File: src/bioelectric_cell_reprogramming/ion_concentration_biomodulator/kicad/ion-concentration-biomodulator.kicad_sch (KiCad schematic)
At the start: 54 parts, among them J1 532610671, J10 39-53-2045, J11 Conn_01x14_Pin, J12 Conn_01x14_Pin, J13 39-53-2045, J14 39-53-2045, J15 Conn_ARM_SWD_TagConnect_TC2030, J16 IPL1-104-01-L-D-K, J17 Conn_01x02_Pin, J18 EJ508A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

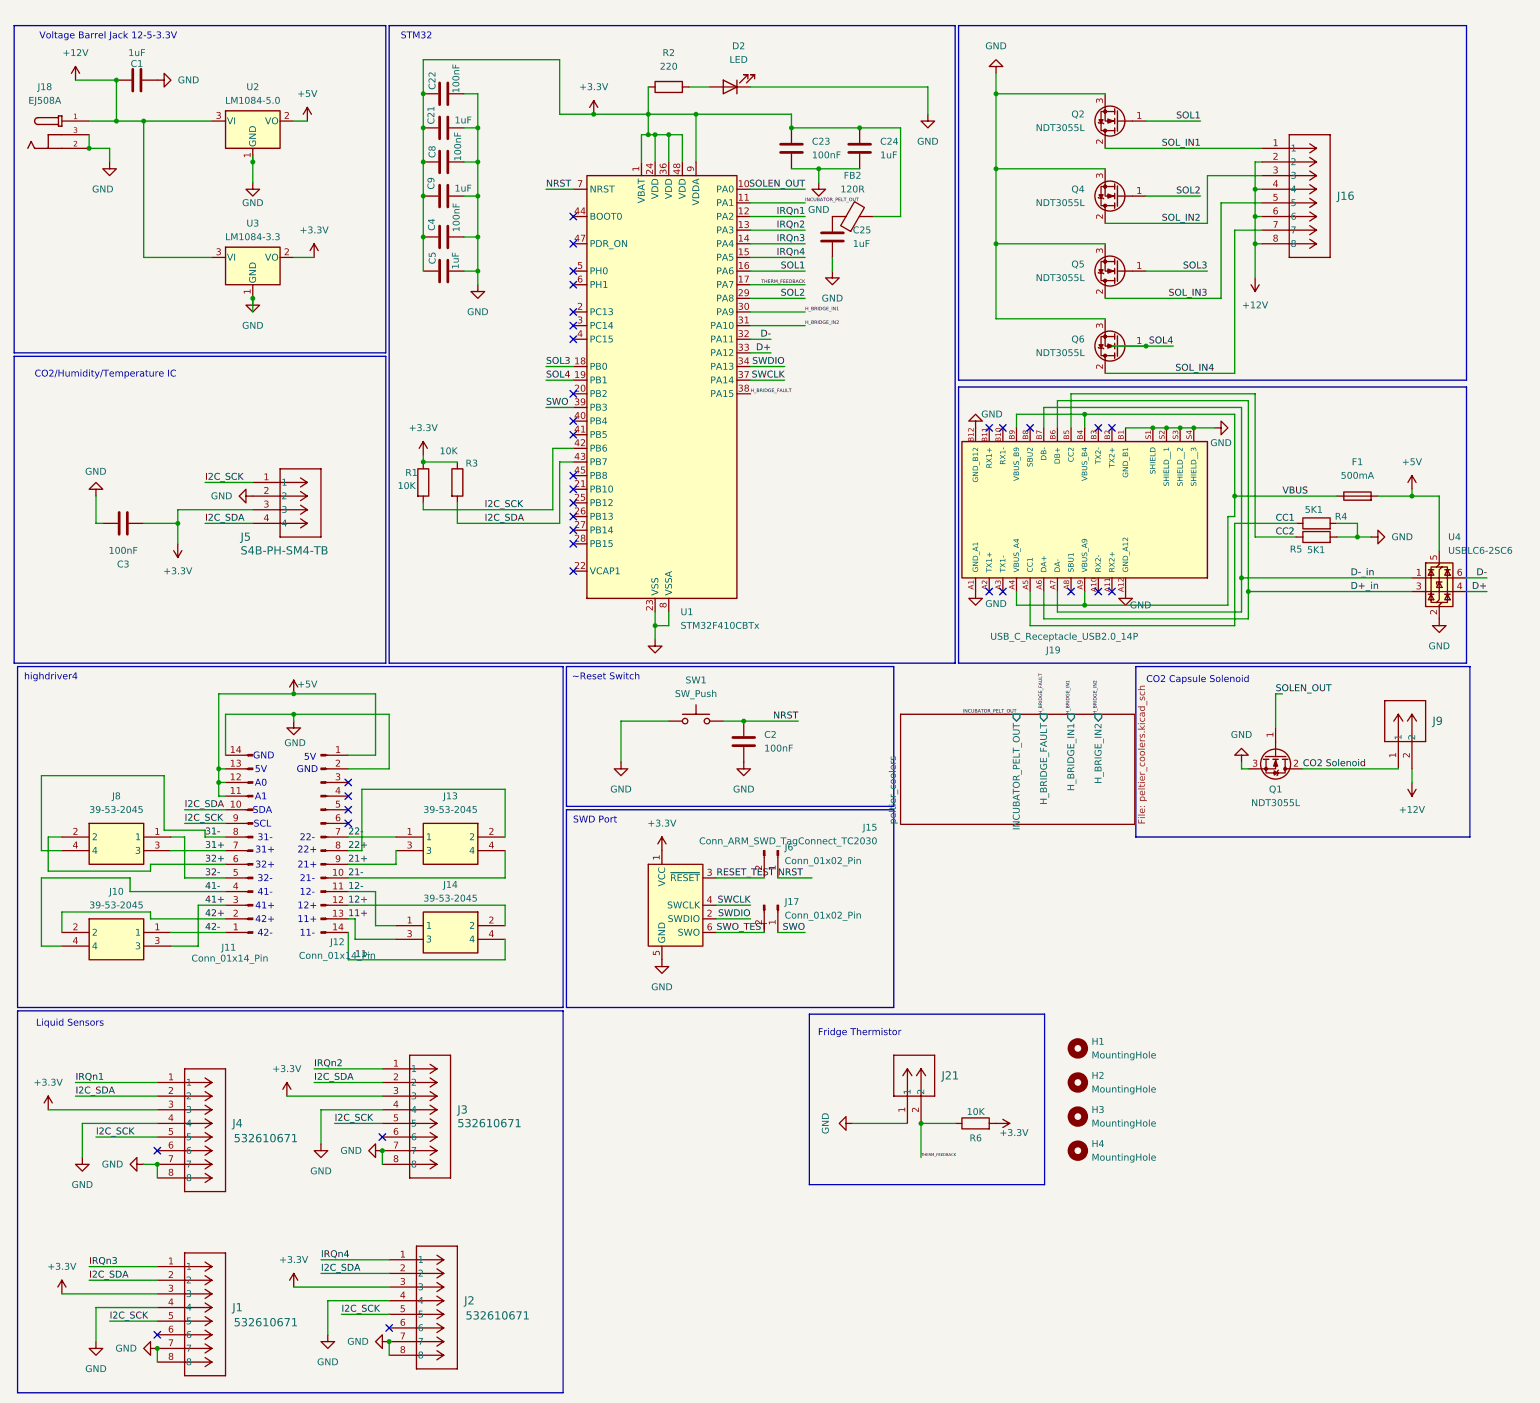
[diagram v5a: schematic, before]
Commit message: fix: bigger STM32, fix mirrored highdriver pinout
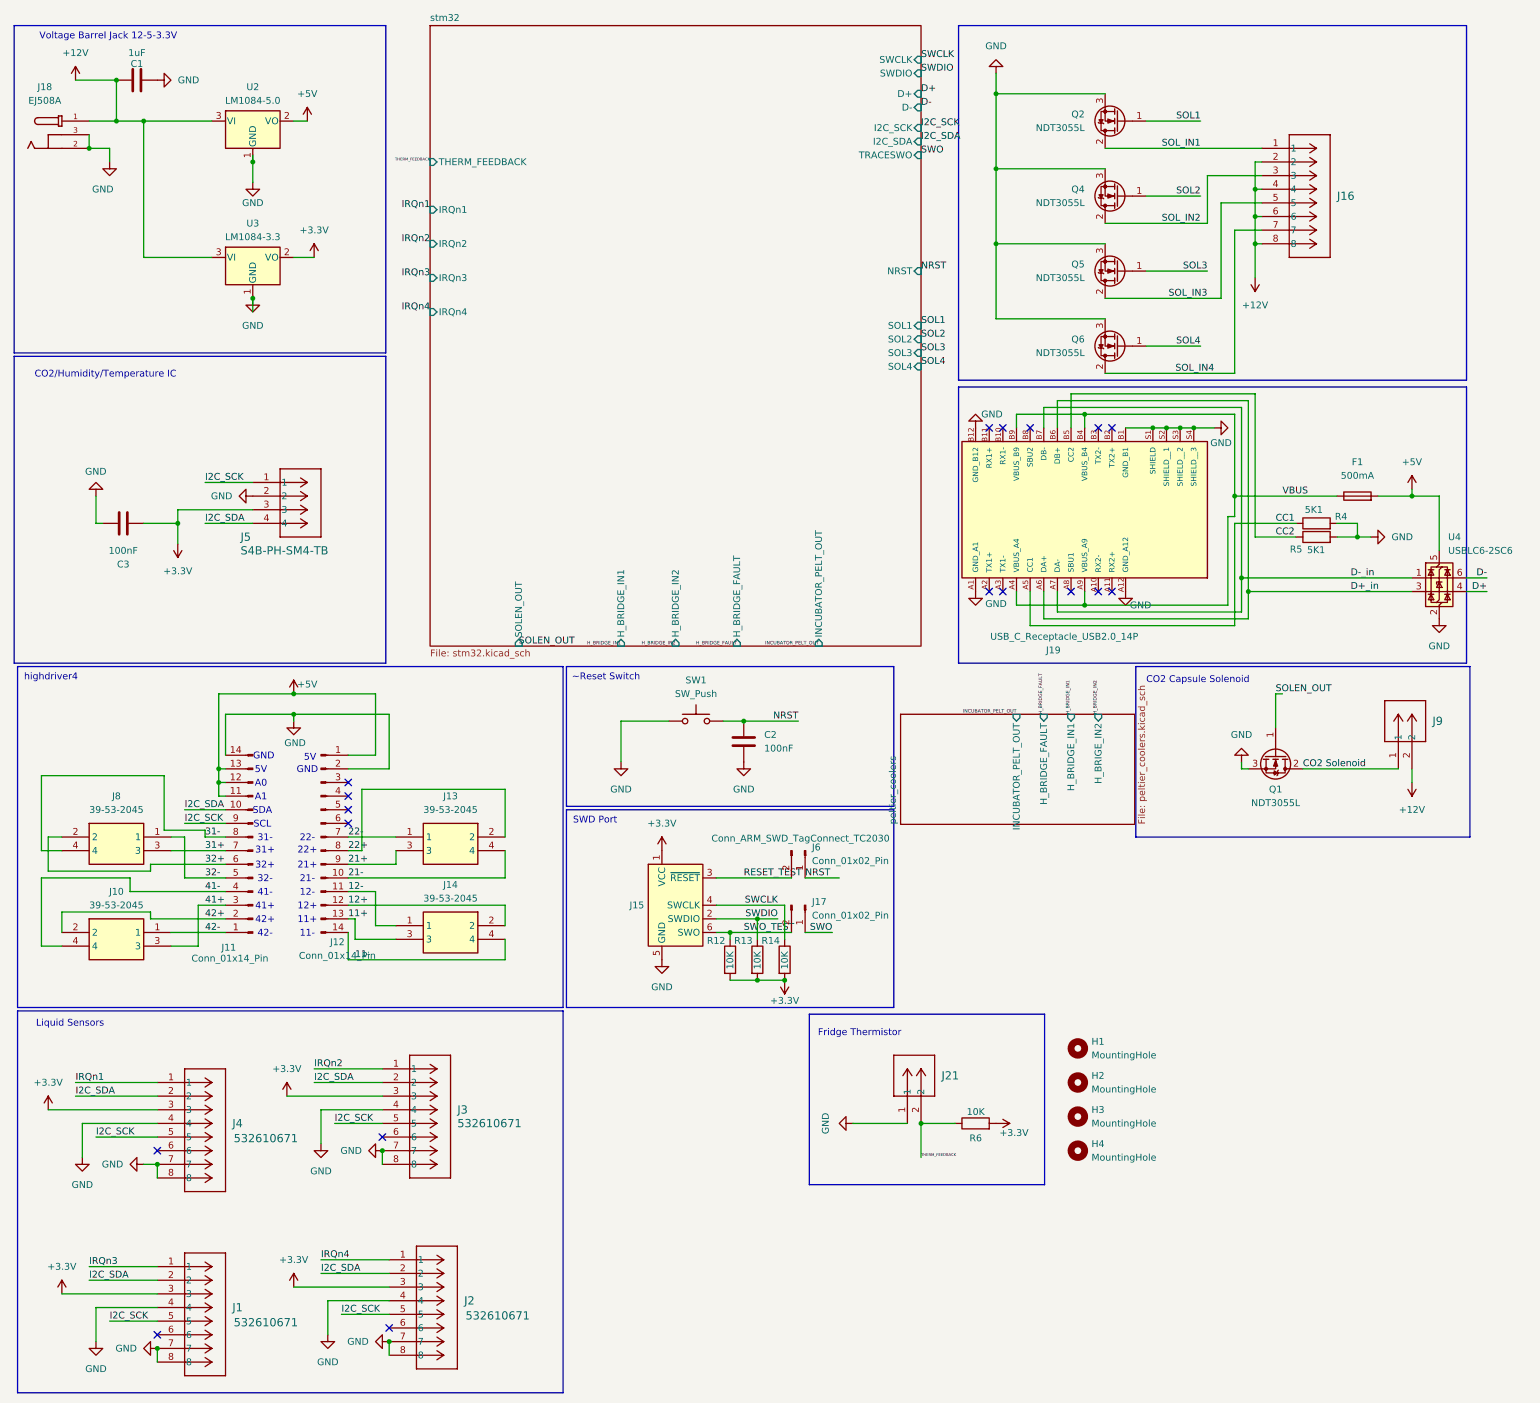
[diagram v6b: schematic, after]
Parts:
- removed C21, C24, C25, C5, C9: 1uF, Capacitor_SMD:C_0201_0603Metric, symbol Device:C
- removed C22, C23, C4, C8: 100nF, Capacitor_SMD:C_0201_0603Metric, symbol Device:C
- removed D2: LED, LED_SMD:LED_0201_0603Metric, symbol Device:LED
- removed FB2: 120R, Inductor_SMD:L_0603_1608Metric, symbol Device:FerriteBead
- removed R1, R3: 10K, Resistor_SMD:R_0201_0603Metric, symbol Device:R
- removed R2: 220, Resistor_SMD:R_0201_0603Metric, symbol Device:R
- removed U1: STM32F410CBTx, Package_QFP:LQFP-48_7x7mm_P0.5mm, symbol MCU_ST_STM32F4:STM32F410CBTx
- added R12, R13, R14: 10K, Resistor_SMD:R_0201_0603Metric, symbol Device:R
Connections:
- net +3.3V: now also R12.2, R13.2, R14.2
- net SWCLK: now also R14.1
- net SWDIO: now also R13.1
- net SWO_TEST: now also R12.1
- no-connect marks 35 -> 18
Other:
- added sheet stm32 (stm32.kicad_sch)
- note removed: "STM32"
- moved on the sheet: J17, J6

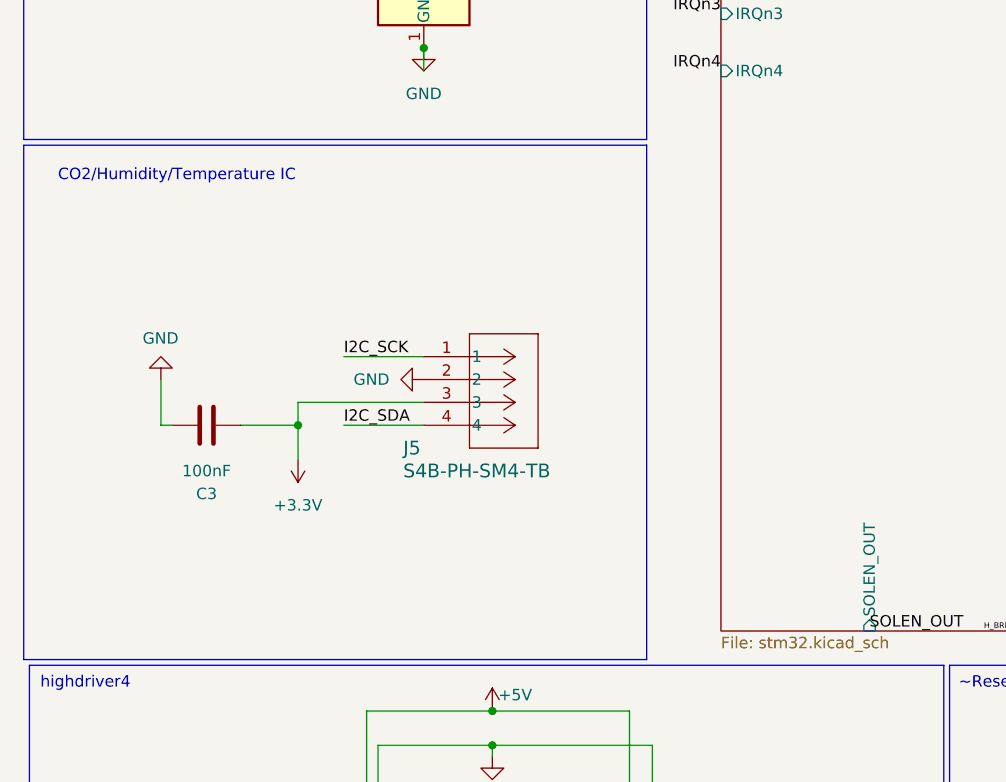
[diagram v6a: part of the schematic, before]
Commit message: fix: new co2 sensor
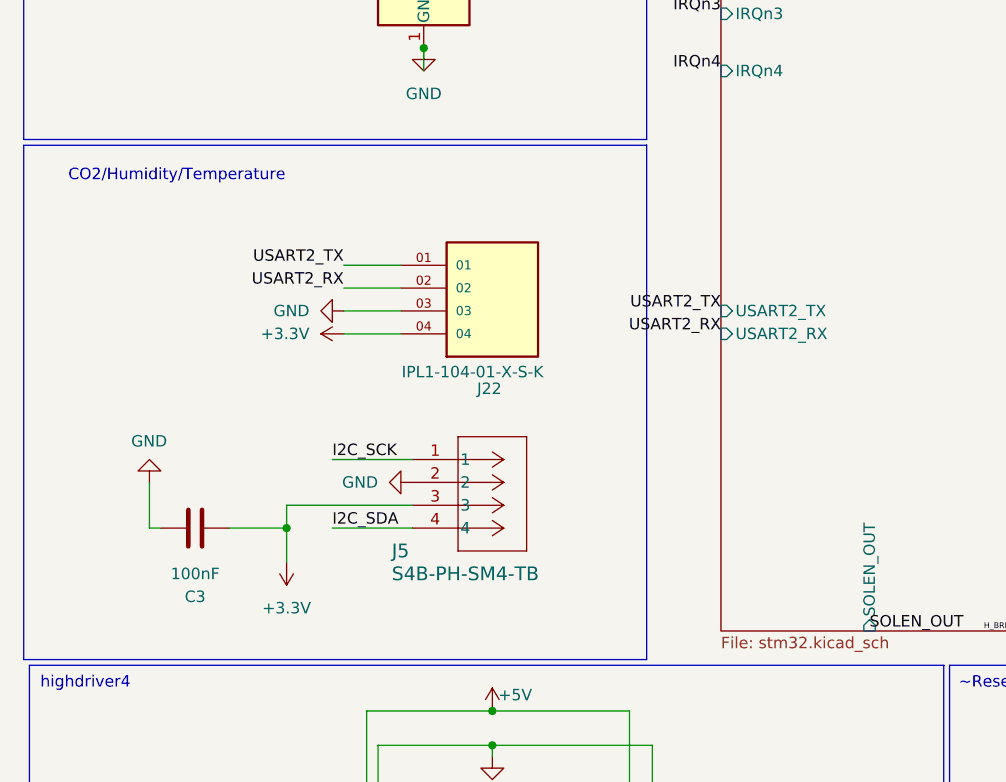
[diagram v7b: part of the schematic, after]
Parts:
- added J22: IPL1-104-01-X-S-K, IPL1_104_01_L_S_K:SAMTEC_IPL1-104-01-X-S-K, symbol IPL1-104-01-X-S-K:IPL1-104-01-X-S-K
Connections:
- net +3.3V: now also J22.04
- net GND: now also J22.03
- new net USART2_RX: J22.02
- new net USART2_TX: J22.01
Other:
- sheet stm32 ports: added USART2_RX, USART2_TX; removed none
- note added: "CO2/Humidity/Temperature"
- note removed: "CO2/Humidity/Temperature IC"
- moved on the sheet: C3, J5

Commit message: feat: oscillator plus mfg files
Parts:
- removed F1: 500mA, Fuse:Fuse_0603_1608Metric, symbol Device:Fuse
- removed J19: USB_C_Receptacle_USB2.0_14P, 12401610E4_2A.pretty:AMPHENOL_12401610E4_2A, symbol 12401610E4_2A:12401610E4_2A
- removed U4: USBLC6-2SC6, Package_TO_SOT_SMD:SOT-23-6, symbol Power_Protection:USBLC6-2SC6
- added USBC1: ~, USB-C-SMD_MC-311D:USB-C-SMD_MC-311D, symbol USB-C-SMD_MC-311D:MC-311D
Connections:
- net +5V: now also USBC1.A4-B9 (VBUS), USBC1.B4-A9 (VBUS)
- net CC1: now also R5.1, USBC1.A5 (CC1); no longer R4.1
- net CC2: now also R4.1, USBC1.B5 (CC2); no longer R5.1
- net D+: now also USBC1.A6 (DP1), USBC1.B6 (DP2)
- net D-: now also USBC1.A7 (DN1), USBC1.B7 (DN2)
- net GND: now also USBC1.1 (SHIELD), USBC1.2 (SHIELD), USBC1.3 (SHIELD), USBC1.4 (SHIELD), USBC1.A1-B12 (GND), USBC1.B1-A12 (GND)
- no-connect marks 18 -> 10
